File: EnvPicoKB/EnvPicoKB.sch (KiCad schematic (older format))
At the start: 53 parts, among them J1 Conn_01x04, J2 SKRKAEE020, J3 2.54mm header 01x20, J4 2.54mm header 01x20, J5 Conn_01x03_Male, U1 TLV75533PDBVR, U3 RP2040, Y1 3225_4P

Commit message: woops, wrong JST connector lol.
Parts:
- J1: footprint Connector_JST:JST_XH_S4B-XH-A-1_1x04_P2.50mm_Horizontal -> Connector_JST:JST_SH_BM04B-SRSS-TB_1x04-1MP_P1.00mm_Vertical
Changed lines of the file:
@@
 F 0 "J1" H 668 1325 50  0000 C CNN
 F 1 "Conn_01x04" H 668 1416 50  0000 C CNN
-F 2 "Connector_JST:JST_XH_S4B-XH-A-1_1x04_P2.50mm_Horizontal" H 750 1750 50  0001 C CNN
+F 2 "Connector_JST:JST_SH_BM04B-SRSS-TB_1x04-1MP_P1.00mm_Vertical" H 750 1750 50  0001 C CNN
 F 3 "~" H 750 1750 50  0001 C CNN
 	1    750  1750

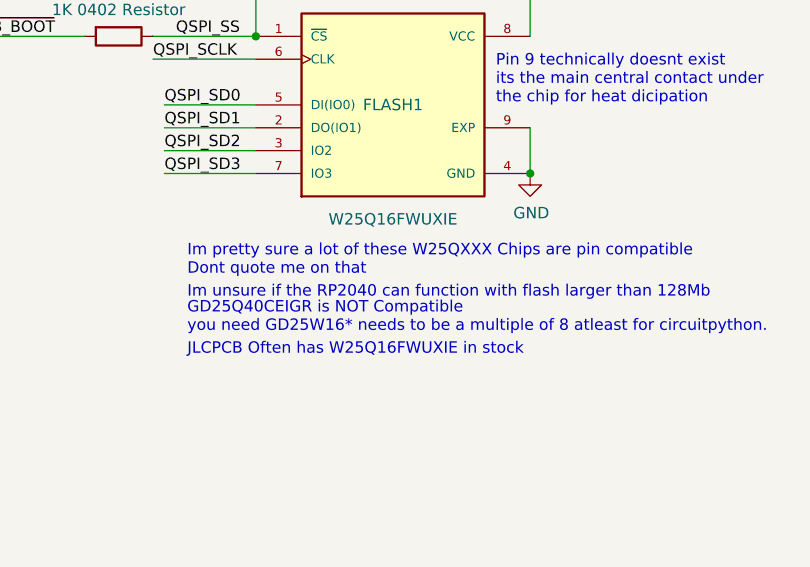
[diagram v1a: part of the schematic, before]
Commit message: corrected a placeholder reference I forgot to label as such, also added more comments in the schematic for the main design.
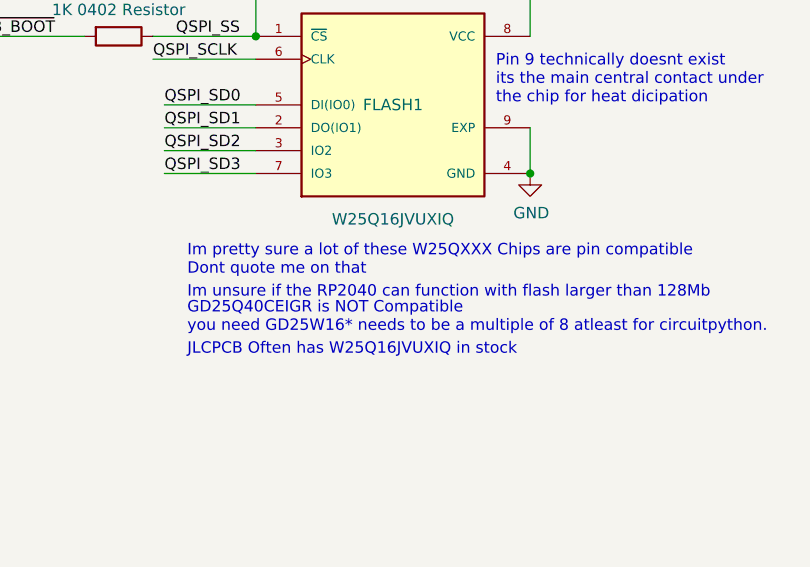
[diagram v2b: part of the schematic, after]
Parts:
- FLASH1: value W25Q16FWUXIE -> W25Q16JVUXIQ
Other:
- note added: "JLCPCB Often has W25Q16JVUXIQ in stock"
- note removed: "JLCPCB Often has W25Q16FWUXIE in stock"
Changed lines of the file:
@@
 P 3100 5250
 F 0 "FLASH1" H 3100 5250 50  0000 C CNN
-F 1 "W25Q16FWUXIE" H 3100 4750 50  0000 C CNN
+F 1 "W25Q16JVUXIQ" H 3100 4750 50  0000 C CNN
 F 2 "Package_SON:SON-8-1EP_3x2mm_P0.5mm_EP1.4x1.6mm" H 3100 5250 50  0001 L BNN
 F 3 "" H 3100 5250 50  0001 L BNN
@@
 Connection ~ 3700 5550
 Text Notes 2200 6350 0    50   ~ 0
-JLCPCB Often has W25Q16FWUXIE in stock
+JLCPCB Often has W25Q16JVUXIQ in stock
 Text Notes 2850 8250 0    50   ~ 0
 not 22pf but pick to match crystal.
